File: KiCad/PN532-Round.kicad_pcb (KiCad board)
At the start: 2 copper layers, 46 x 46 mm, 52 parts, among them J1 Bell, J2 SPOX, SW1 TAMPER, U1 PN532, U2 QR, U3 QR, Y1 27.12MHz

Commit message: New antenna design
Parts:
- moved AJK1 1.12 mm to (89.1, 91.1)
- moved D1 1.00 mm to (113.0, 105.0)
- moved D2 1.00 mm to (113.0, 100.0)
- moved D3 1.00 mm to (113.0, 95.0)
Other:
- rule pad_to_mask_clearance: 0 -> 0.01

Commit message: Better antennna
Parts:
- removed U3: QR, RevK:QR-PN532
- added J2: Bell, RevK:PinHeader_1x02_P2.54mm_Vertical_SMD_Pin1Left, F.Cu at (92.0, 108.0)
- J1: footprint RevK:PinHeader_1x02_P2.54mm_Vertical -> RevK:PinHeader_1x02_P2.54mm_Vertical_SMD_Pin1Right
- J3: renamed from J2; footprint RevK:Molex_MiniSPOX_H4V -> RevK:PinHeader_1x04_P2.54mm_Vertical_SMD_Pin1Right
- moved U2 2.50 mm to (100.0, 112.5), turned to 90 degrees
- moved J1 1.84 mm to (108.0, 108.0), turned to 180 degrees
- moved J3 1.04 mm to (100.0, 106.5), turned to 90 degrees
- moved AJK1 1.00 mm to (89.1, 92.1)
- moved D1 0.50 mm to (112.5, 105.0)
- moved D2 0.50 mm to (112.5, 100.0)
- moved D3 0.50 mm to (112.5, 95.0)
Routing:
- net GND: track 92.6 -> 127.3 mm, vias 13 -> 14
- net Net-(J2-Pad2): track 1.32 -> 21.1 mm
- net Net-(J1-Pad2): track 0.00 -> 8.38 mm
- net Net-(D1-Pad2): track 1.40 -> 6.97 mm
- net Net-(D3-Pad2): track 5.52 -> 9.25 mm
- net +5V: track 25.3 -> 28.8 mm, vias 3 -> 4
- net Net-(D2-Pad2): track 14.6 -> 12.0 mm
- net +3V3: track 92.4 -> 90.9 mm
- net Net-(J3-Pad4): track 8.42 -> 7.64 mm, vias 1 -> 0
- net Net-(D6-Pad6): track 10.8 -> 10.1 mm, vias 0 -> 2
- net Net-(C19-Pad1): track 18.1 -> 18.6 mm, vias 0 -> 2
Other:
- board text removed: "${URL}"

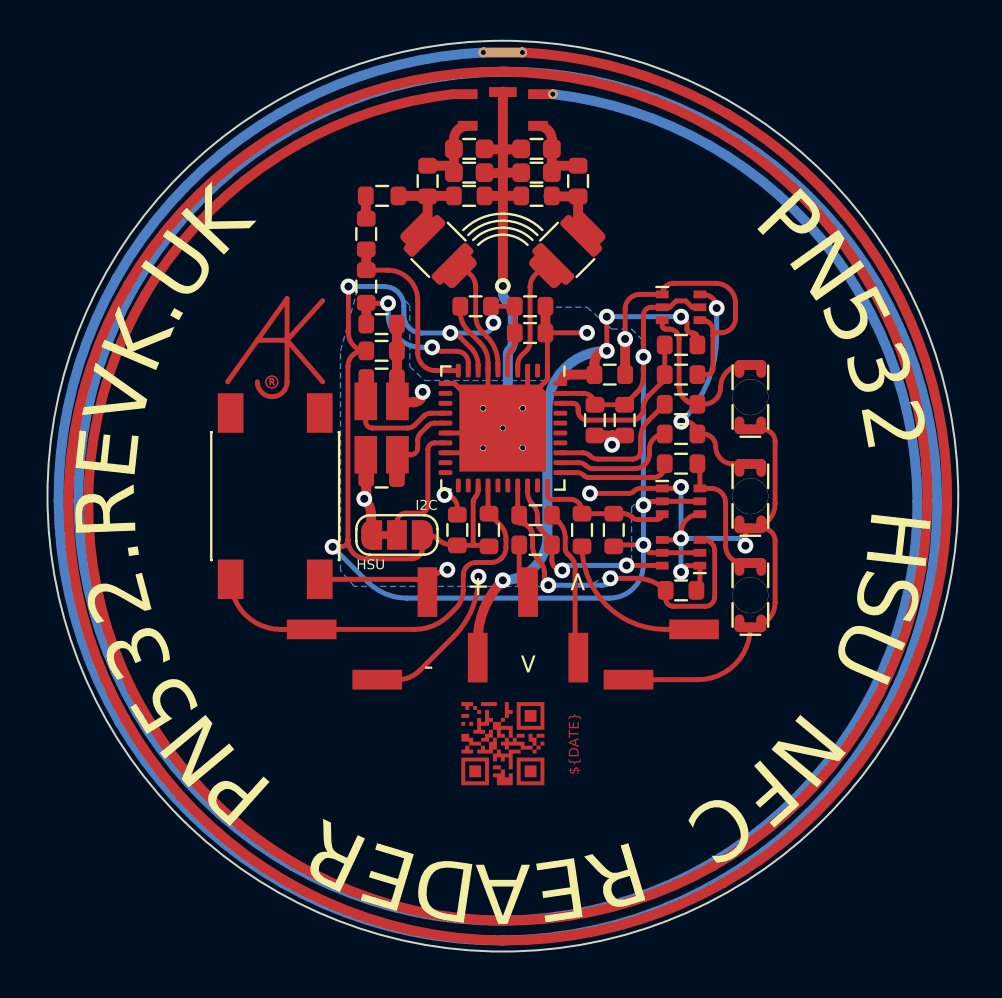
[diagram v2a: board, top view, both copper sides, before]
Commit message: Tweak screw holes, and tidy round PCB
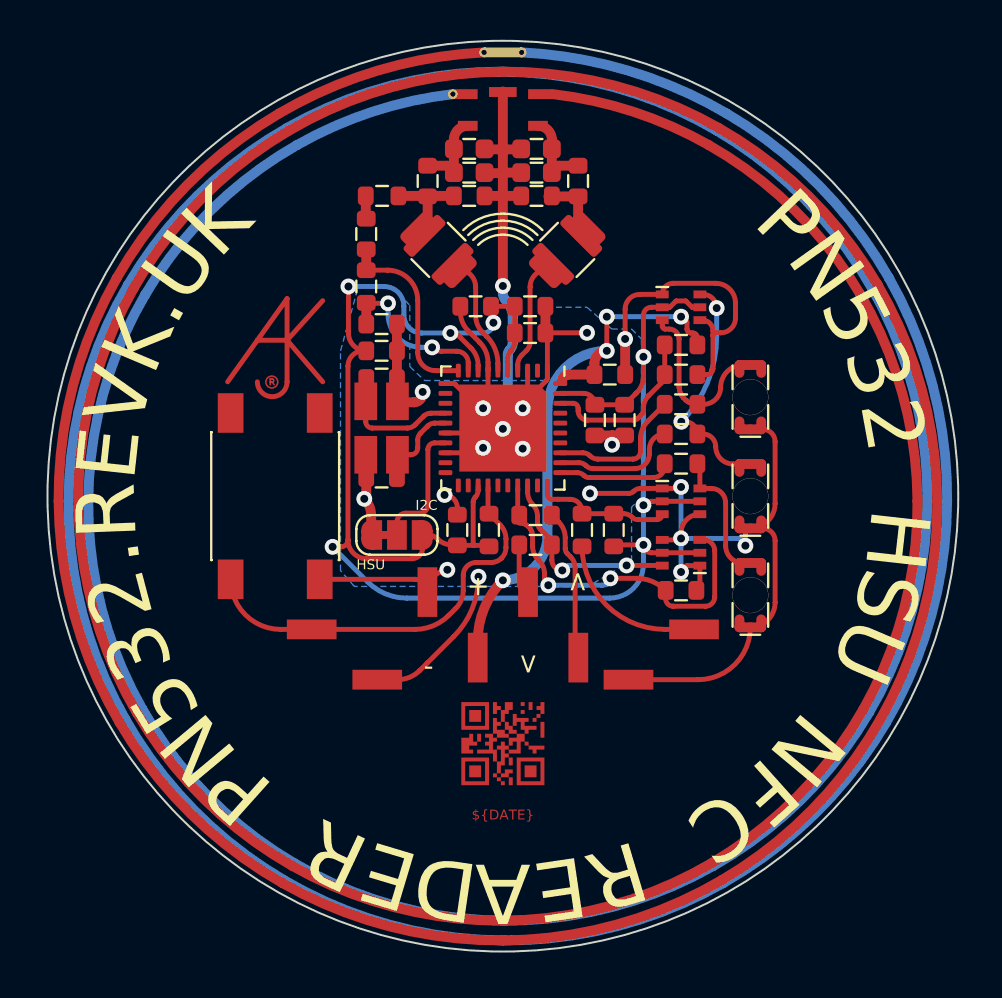
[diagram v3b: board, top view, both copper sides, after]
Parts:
- moved R3 0.23 mm to (101.8, 80.5)
- moved R1 0.21 mm to (98.2, 80.5)
- turned U2 to 0 degrees
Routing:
- net GND: vias 14 -> 19

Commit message: Tidy up and new case
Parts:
- C1, C2: value 160pF 1% -> 160pF; footprint RevK:Cx2_0603 -> RevK:C_0603
- C11, C12, C14, C18, C7, C9: value 0.1uF -> 100nF
- C3, C4: value 22pF 1% -> 22pF
- C8: value 1nF 2% -> 1nF
- J3: value SPOX -> 0.1"
- R1, R3: footprint RevK:Hidden -> RevK:R_0603_
- R2: footprint RevK:Hidden -> RevK:R_0805_
- moved C1 0.84 mm to (101.7, 83.3)
- moved C2 0.84 mm to (98.3, 83.3)
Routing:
- net GND: track 127.3 -> 125.5 mm
- net Net-(A1-Pad1): track 4.25 -> 3.71 mm
- net Net-(A1-Pad3): track 4.25 -> 3.71 mm
